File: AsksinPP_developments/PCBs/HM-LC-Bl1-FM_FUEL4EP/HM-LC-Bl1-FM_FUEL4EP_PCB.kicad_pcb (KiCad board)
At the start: 2 copper layers, 124.5 x 96.7 mm, 69 parts, among them J1 Down Button, J10 charge, J11 24V PSU, J12 230V Netzteil Relais, J13 Velux Motor, J14 Motor direction LEDs, J15 Charge Indication LED, J16 H Brücke Relais In, J17 Motor Relais In, J18 Conn_01x03, J19 GND, J2 Up Button, J3 Dual LED, J4 Config Button, J5 ISP Programmer, J6 Accumulator, J7 LED rot, J8 LED grün, J9 LED gelb, Q1 IRLU024N, Q2 BD238, Q3 IRF9Z34N, Q4 2N7000, Q5 MCP1702-2802E_TO

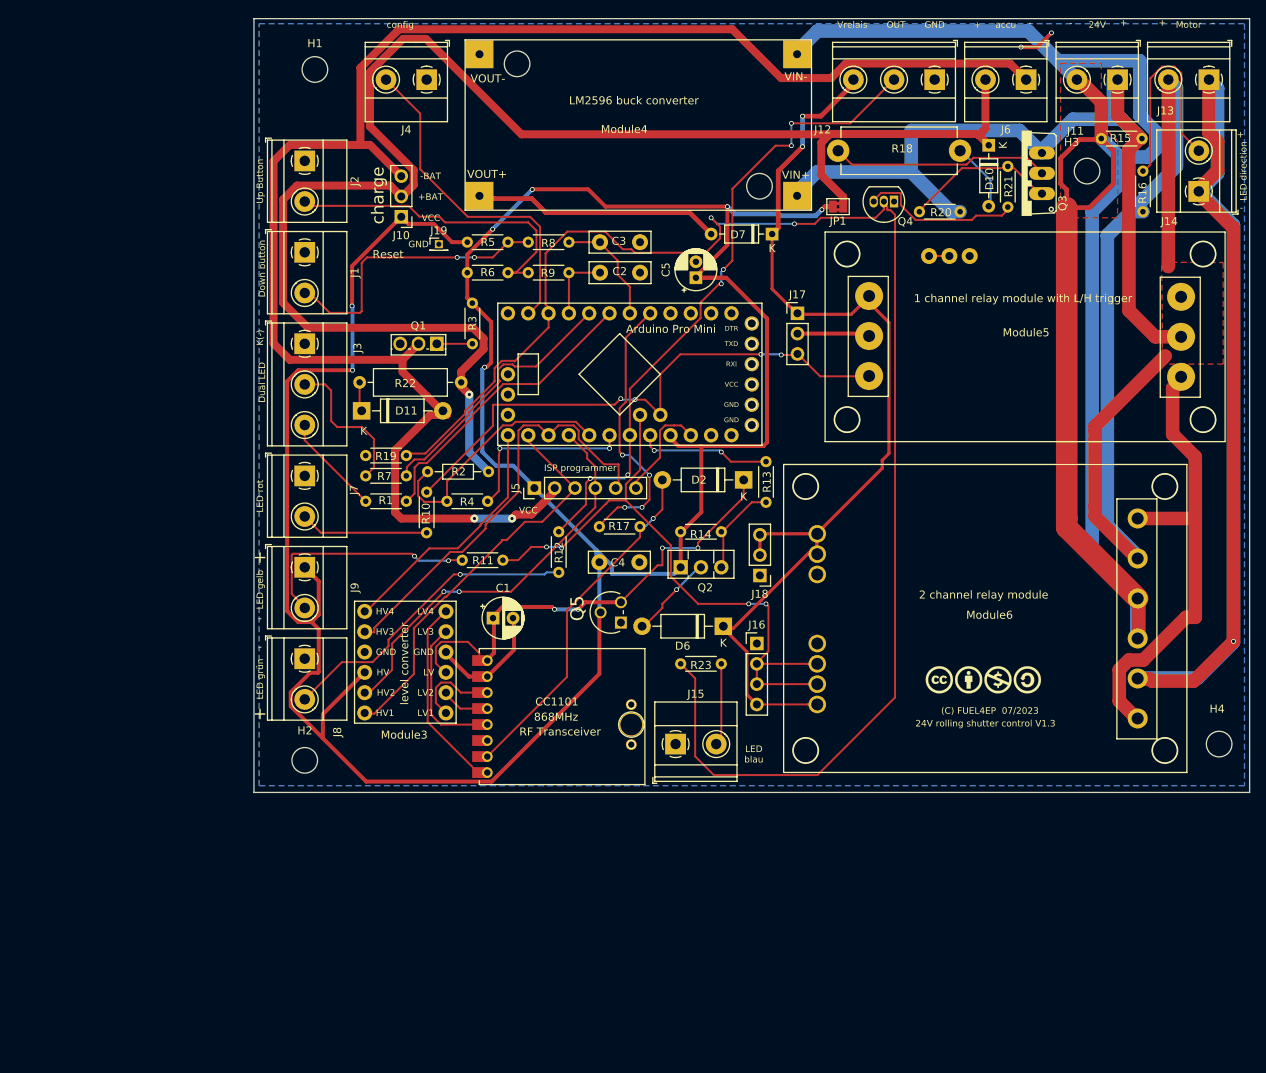
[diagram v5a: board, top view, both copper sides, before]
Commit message: PCBs: KiCAD6 required improvements of layout data bases; added E07-900M10S into FUEL and footprint library
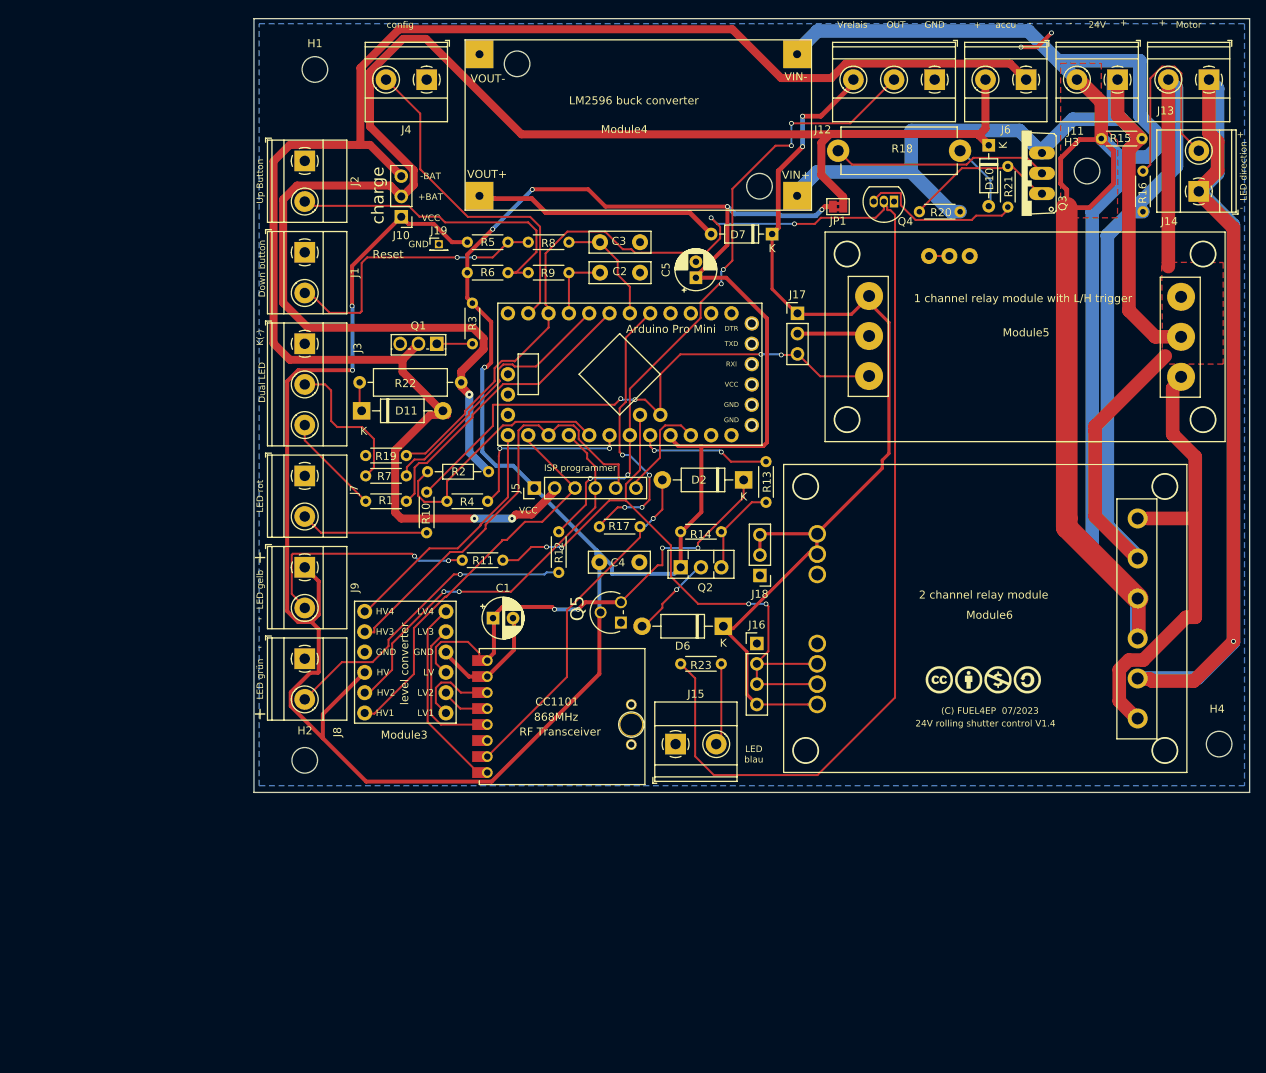
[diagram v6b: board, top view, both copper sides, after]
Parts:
- Module3: value >VALUE -> 4_channel_LOGIC_LEVEL_CONVERTER
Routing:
- net VCC: track 345.3 -> 341.0 mm
- net /V_relais: track 131.6 -> 130.2 mm
- net Net-(D7-Pad2): track 33.4 -> 32.2 mm
- net Net-(J15-Pad2): track 10.4 -> 9.52 mm
- net Net-(J2-Pad2): track 40.3 -> 39.6 mm
- net /MOSI: track 50.5 -> 49.7 mm
- net /RSET: track 13.1 -> 12.4 mm
- net /MISO: track 54.3 -> 53.8 mm
- net Net-(Q3-Pad1): track 18.8 -> 18.3 mm
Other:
- board text added: "(C) FUEL4EP 07/2023 24V rolling shutter control V1.4"
- board text added: "24V rolling shutter control V1.4"
- board text removed: "(C) FUEL4EP 07/2023 24V rolling shutter control V1.3"
- board text removed: "24V rolling shutter control V1.3"

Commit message: PCBs: Fixes to ensure a proper production at JLCPCB, e.g. corrections of origins, rotations of assembled ICs etc.
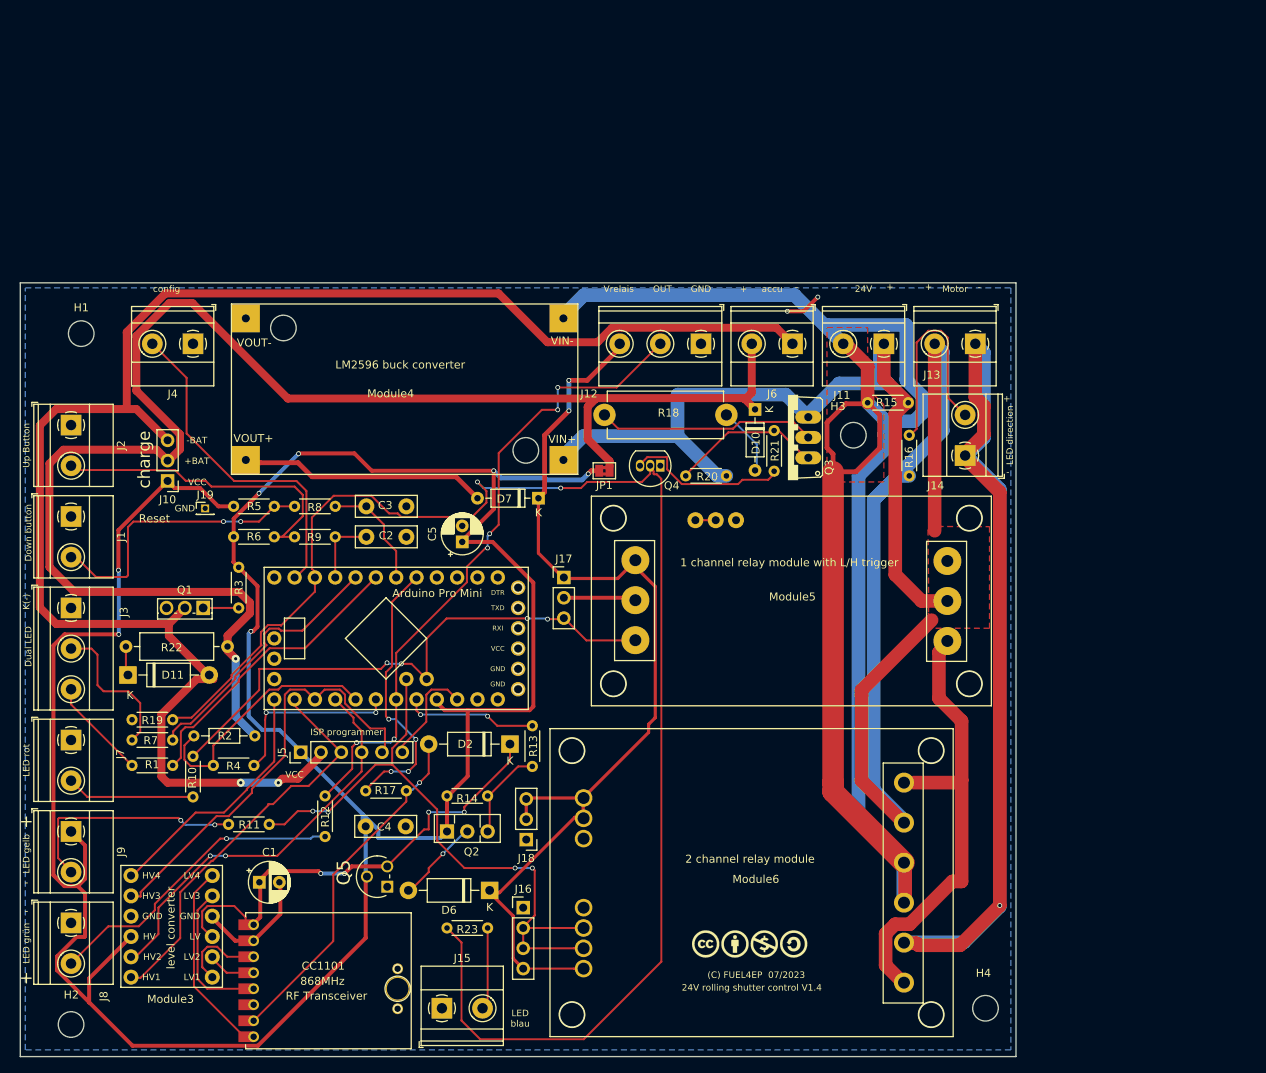
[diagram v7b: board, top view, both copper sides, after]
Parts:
- moved C1 44.1 mm to (29.9, 74.9)
- moved R12 44.1 mm to (38.1, 64.1)
- moved R14 44.1 mm to (53.3, 64.1)
- moved R21 44.1 mm to (94.2, 18.5)
- moved C2 44.1 mm to (43.3, 31.8)
- moved C3 44.1 mm to (43.3, 27.9)
- moved C4 44.1 mm to (43.2, 67.9)
- moved C5 44.1 mm to (55.2, 32.4)
- moved D2 44.1 mm to (61.2, 57.7)
- moved D6 44.1 mm to (58.7, 75.9)
- moved D7 44.1 mm to (64.8, 26.9)
- moved H2 44.1 mm to (6.35, 92.7)
- moved H4 44.1 mm to (120.7, 90.7)
- moved J1 44.1 mm to (6.35, 29.2)
- moved J10 44.1 mm to (18.4, 24.8)
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
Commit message: HM-LC-Bl1-FM_FUEL4EP and HB-UNI-SenAct-4-4-SC_DS_FUEL4EP: fix of MCP1702 from 2.8V to 3.3V version
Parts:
- Module3: value 4_channel_LOGIC_LEVEL_CONVERTER -> >VALUE
- Q5: value MCP1702-2802E_TO -> MCP1702-3302E/TO
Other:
- board text added: "(C) FUEL4EP 07/2023 24V rolling shutter control V1.5"
- board text removed: "(C) FUEL4EP 07/2023 24V rolling shutter control V1.4"
